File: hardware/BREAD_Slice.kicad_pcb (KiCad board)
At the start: 2 copper layers, 70 x 100 mm, 54 parts, among them J1 1985195, J4 Conn_01x10_Socket, J5 1990106, J6 1990106, Q1 NTGS4111PT1G, SW1 SW_SPDT, SW2 SW_DIP_x04, U1 AP63205, U2 LTV-817S, U3 LTV-817S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

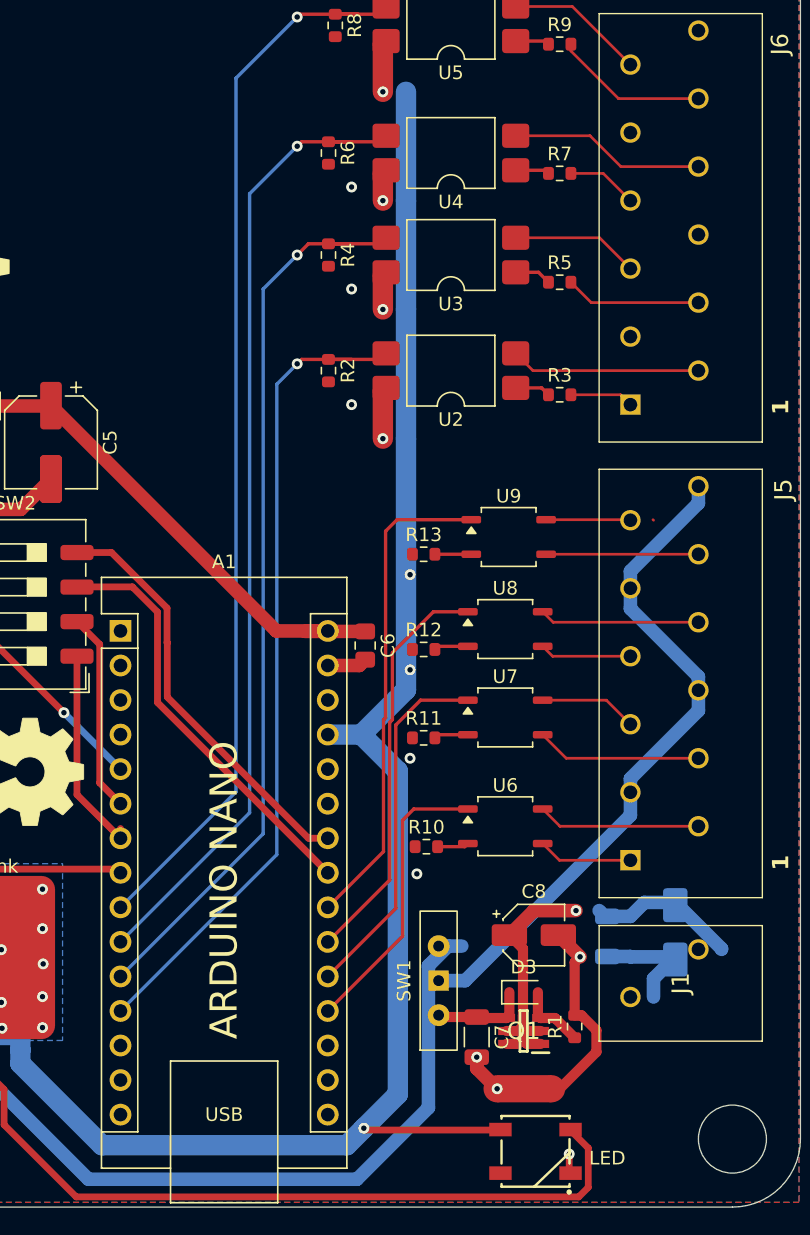
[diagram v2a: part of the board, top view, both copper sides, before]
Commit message: rerouted again with new kml library
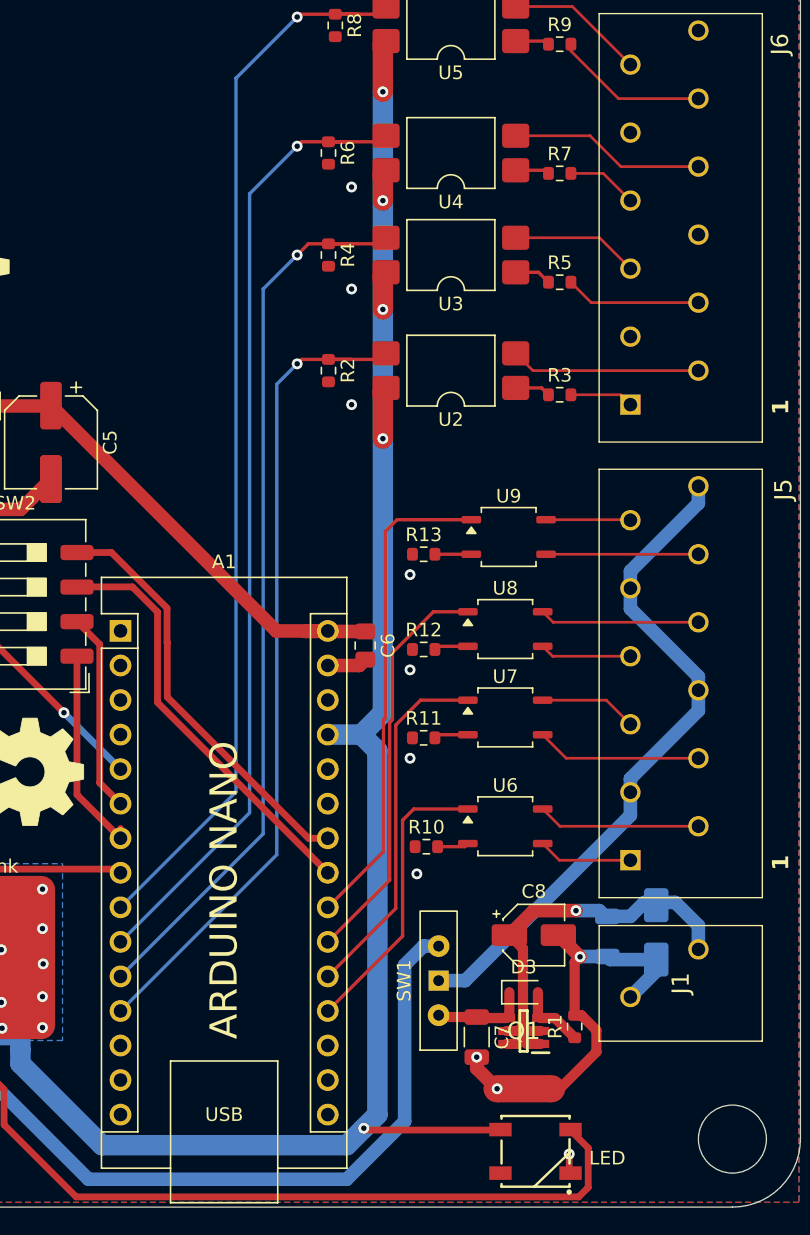
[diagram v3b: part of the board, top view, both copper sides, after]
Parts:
- moved D4 1.40 mm to (182.0, 119.6)
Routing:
- net +5V: track 157.7 -> 155.7 mm
- net +12V: track 118.5 -> 117.4 mm
- net /Input Power Protection/INPUT_VDD: track 32.1 -> 33.1 mm
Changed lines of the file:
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@@
 	(footprint "Diode_SMD:D_SMA"
 		(layer "B.Cu")
-		(at 183.4 119.6 -90)
+		(at 182 119.6 -90)
 		(descr "Diode SMA (DO-214AC)")
 		(tags "Diode SMA (DO-214AC)")
@@
 	)
 	(segment
-		(start 123.95 102.3)
-		(end 126.525 104.875)
-		(width 1.5)
+		(start 140.25 137.75)
+		(end 159.25 137.75)
+		(width 1)
 		(layer "B.Cu")
 		(net 4)
 	)
 	(segment
-		(start 165.25 122.05)
-		(end 166.69 120.61)
-		(width 1)
+		(start 123.95 102.3)
+		(end 126.525 104.875)
+		(width 1.5)
 		(layer "B.Cu")
 		(net 4)
@@
 	)
 	(segment
-		(start 160 137.75)
-		(end 165.25 132.5)
-		(width 1)
-		(layer "B.Cu")
-		(net 4)
-	)
-	(segment
 		(start 126.2 80.89)
 		(end 125.56 80.89)
@@
 	)
 	(segment
-		(start 125.25 123.901649)
-		(end 125.25 127.25)
+		(start 127.34665 121.804999)
+		(end 125.25 123.901649)
+		(width 1)
+		(layer "B.Cu")
+		(net 4)
+	)
+	(segment
+		(start 163.5 133.5)
+		(end 163.5 122)
 		(width 1)
 		(layer "B.Cu")
@@
 	)
 	(segment
+		(start 125.25 123.901649)
+		(end 125.25 127.25)
+		(width 1)
+		(layer "B.Cu")
+		(net 4)
+	)
+	(segment
 		(start 127.6125 119.7875)
 		(end 127.325 119.5)
@@
 	)
 	(segment
-		(start 166.69 120.61)
-		(end 167.7 120.61)
+		(start 127.6125 121.805)
+		(end 127.6125 119.7875)
 		(width 1)
 		(layer "B.Cu")
@@
 	)
 	(segment
-		(start 127.6125 121.805)
-		(end 127.6125 119.7875)
+		(start 131.101 128.601)
+		(end 140.25 137.75)
 		(width 1)
 		(layer "B.Cu")
@@
 	)
 	(segment
-		(start 126.5 128.5)
-		(end 128.305083 128.5)
-		(width 1)
+		(start 126.525 104.875)
+		(end 126.525 118.7)
+		(width 1.5)
 		(layer "B.Cu")
 		(net 4)
 	)
 	(segment
-		(start 131.101 128.601)
-		(end 140.25 137.75)
+		(start 163.5 122)
+		(end 164.89 120.61)
 		(width 1)
 		(layer "B.Cu")
@@
 	)
 	(segment
-		(start 126.525 104.875)
-		(end 126.525 118.7)
-		(width 1.5)
+		(start 125.25 127.25)
+		(end 126.5 128.5)
+		(width 1)
 		(layer "B.Cu")
 		(net 4)
@@
 	)
 	(segment
-		(start 127.34665 121.804999)
-		(end 125.25 123.901649)
-		(width 1)
-		(layer "B.Cu")
-		(net 4)
-	)
-	(segment
 		(start 128.406083 128.601)
 		(end 131.101 128.601)
@@
 	)
 	(segment
-		(start 125.25 127.25)
-		(end 126.5 128.5)
+		(start 164.89 120.61)
+		(end 166 120.61)
+		(width 1)
+		(layer "B.Cu")
+		(net 4)
+	)
+	(segment
+		(start 159.25 137.75)
+		(end 163.5 133.5)
 		(width 1)
 		(layer "B.Cu")
@@
 	)
 	(segment
-		(start 165.25 132.5)
-		(end 165.25 122.05)
-		(width 1)
-		(layer "B.Cu")
-		(net 4)
-	)
-	(segment
-		(start 140.25 137.75)
-		(end 160 137.75)
+		(start 126.5 128.5)
+		(end 128.305083 128.5)
 		(width 1)
 		(layer "B.Cu")
@@
 	)
 	(segment
-		(start 163 107.75)
-		(end 160.31 105.06)
-		(width 1.5)
-		(layer "B.Cu")
-		(net 5)
-	)
-	(segment
 		(start 135.3 116.48)
 		(end 135.3 119.43)
@@
 	)
 	(segment
-		(start 163 131.5)
-		(end 163 107.75)
-		(width 1.5)
-		(layer "B.Cu")
-		(net 5)
-	)
-	(segment
-		(start 163.6 73.8)
-		(end 163.6 65.8)
-		(width 1.5)
-		(layer "B.Cu")
-		(net 5)
-	)
-	(segment
 		(start 135.3 119.43)
 		(end 135.325 119.455)
@@
 	)
 	(segment
-		(start 163.6 101.77)
-		(end 163.6 83.3)
+		(start 161.9 103.47)
+		(end 160.31 105.06)
 		(width 1.5)
 		(layer "B.Cu")
@@
 	)
 	(segment
-		(start 160.5 134)
-		(end 163 131.5)
-		(width 1.5)
-		(layer "B.Cu")
-		(net 5)
-	)
-	(segment
 		(start 159.25 135.25)
 		(end 141.25 135.25)
@@
 	)
 	(segment
-		(start 163.6 65.8)
-		(end 163.6 57.8)
-		(width 1.5)
-		(layer "B.Cu")
-		(net 5)
-	)
-	(segment
-		(start 160.31 105.06)
-		(end 163.6 101.77)
+		(start 160.5 134)
+		(end 161.5 133)
 		(width 1.5)
 		(layer "B.Cu")
@@
 	)
 	(segment
-		(start 163.6 83.3)
-		(end 163.6 73.8)
+		(start 160.5 134)
+		(end 159.25 135.25)
 		(width 1.5)
 		(layer "B.Cu")
@@
 	)
 	(segment
-		(start 160.5 134)
-		(end 159.25 135.25)
+		(start 161.9 57.8)
+		(end 161.9 103.47)
+		(width 1.5)
+		(layer "B.Cu")
+		(net 5)
+	)
+	(segment
+		(start 161.5 133)
+		(end 161.5 106.25)
+		(width 1.5)
+		(layer "B.Cu")
+		(net 5)
+	)
+	(segment
+		(start 161.5 106.25)
+		(end 160.31 105.06)
 		(width 1.5)
 		(layer "B.Cu")
@@
 	)
 	(segment
+		(start 177.8 118)
+		(end 176.1 118)
+		(width 1)
+		(layer "B.Cu")
+		(net 43)
+	)
+	(segment
 		(start 183.4 117.4)
 		(end 181.125 117.4)
@@
 	)
 	(segment
-		(start 186.8 120.85)
-		(end 186.8 120.8)
+		(start 183.4 117.4)
+		(end 185.1 119.1)
 		(width 1)
 		(layer "B.Cu")
@@
 	)
 	(segment
-		(start 186.8 120.8)
-		(end 183.4 117.4)
+		(start 185.1 119.1)
+		(end 185.1 120.85)
 		(width 1)
 		(layer "B.Cu")
@@
 	)
 	(segment
-		(start 181.8 124.35)
-		(end 181.8 123)
+		(start 176.425 121.375)
+		(end 176.4 121.4)
 		(width 1)
 		(layer "B.Cu")
@@
 	)
 	(segment
-		(start 183.4 121.4)
-		(end 180.125 121.4)
+		(start 182 121.6)
+		(end 182 122.45)
 		(width 1)
 		(layer "B.Cu")
@@
 	)
 	(segment
-		(start 178.125 121.375)
-		(end 178.1 121.4)
+		(start 182 121.6)
+		(end 178.625 121.6)
 		(width 1)
 		(layer "B.Cu")
@@
 	)
 	(segment
-		(start 181.8 123)
-		(end 183.4 121.4)
+		(start 178.625 121.6)
+		(end 178.4 121.375)
 		(width 1)
 		(layer "B.Cu")
@@
 	)
 	(segment
-		(start 180.1 121.375)
+		(start 178.1 121.4)
 		(end 178.125 121.375)
 		(width 1)
@@
 	)
 	(segment
-		(start 180.125 121.4)
-		(end 180.1 121.375)
+		(start 178.4 121.375)
+		(end 176.425 121.375)
+		(width 1)
+		(layer "B.Cu")
+		(net 44)
+	)
+	(segment
+		(start 182 122.45)
+		(end 180.1 124.35)
 		(width 1)
 		(layer "B.Cu")
@@
 		(width 0.2)
 		(layer "F.Cu")
-		(net 50)
-	)
-	(segment
-		(start 181.76 89.26)
-		(end 181.8 89.3)
-		(width 0.2)
-		(layer "F.Cu")

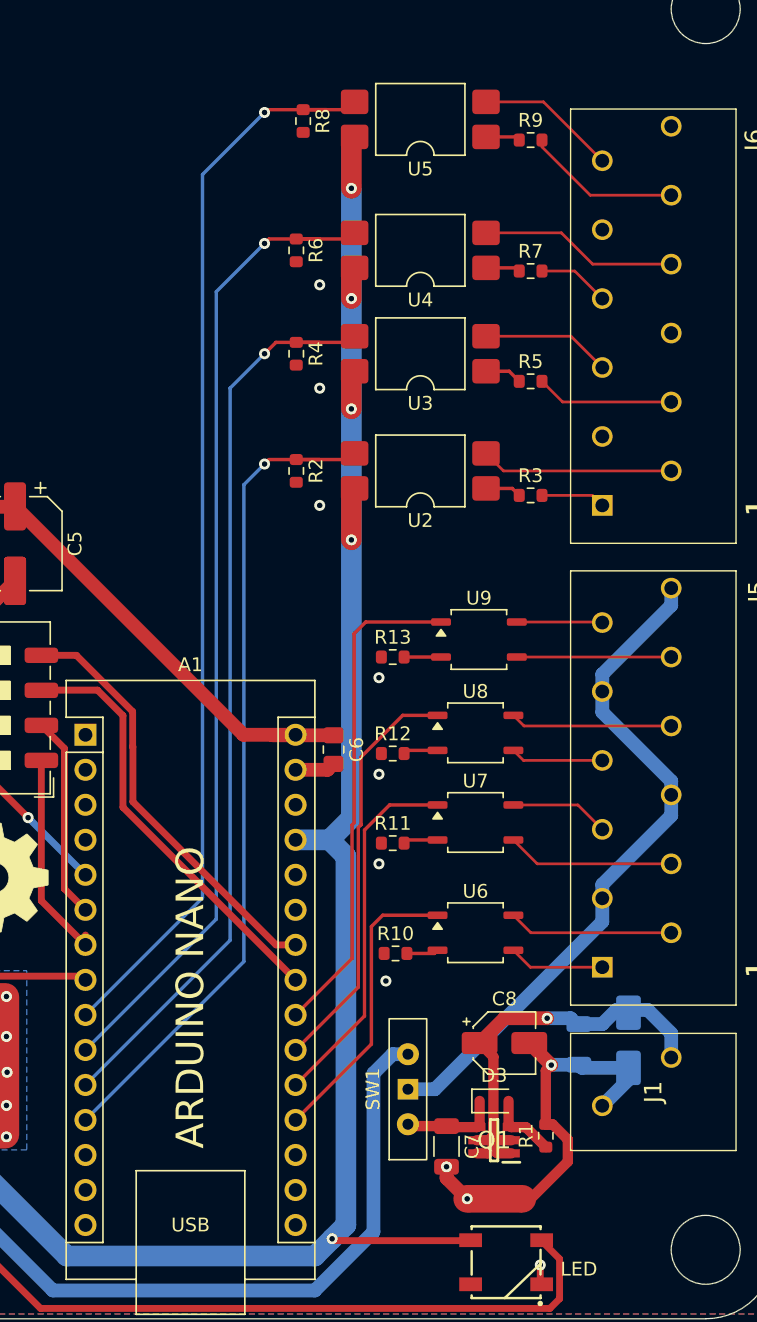
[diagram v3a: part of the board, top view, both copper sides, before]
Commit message: update all to KMLib, untrack backups in gitignore, and revise routing on board to simplify
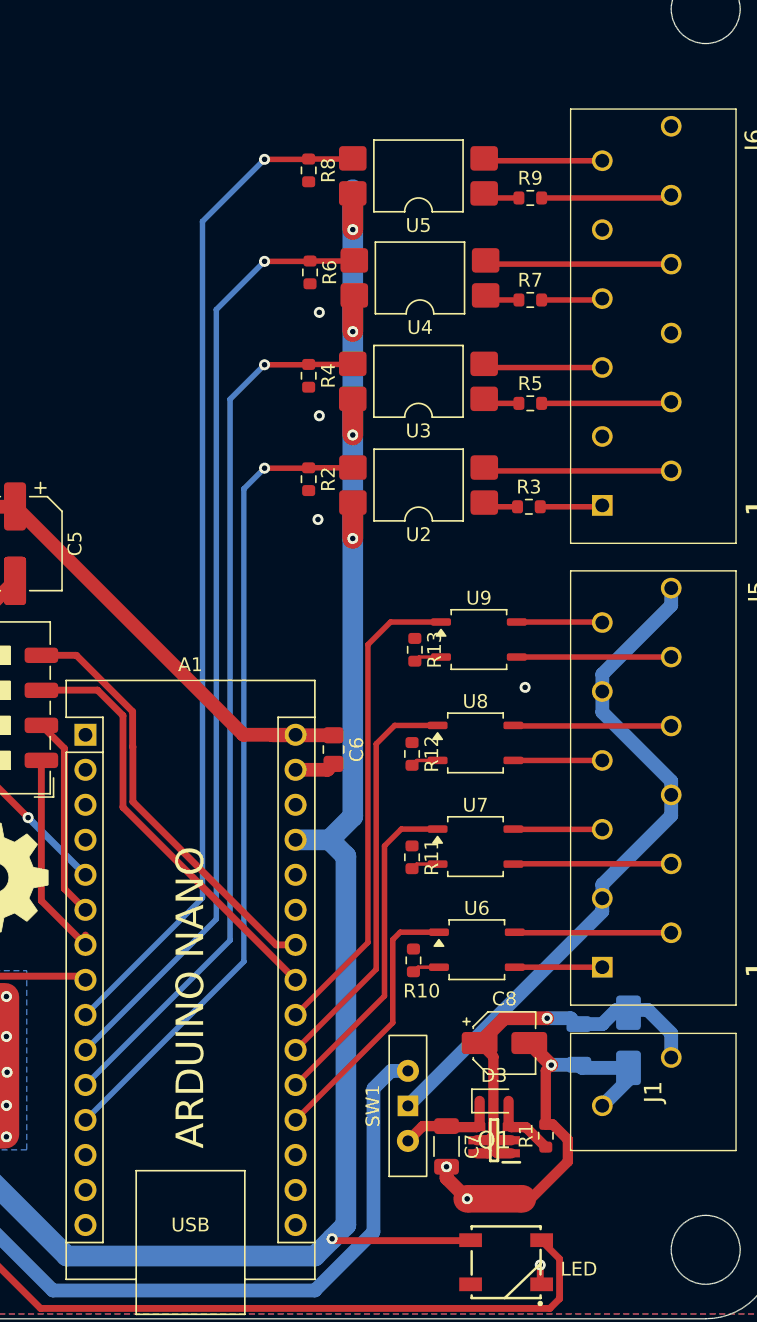
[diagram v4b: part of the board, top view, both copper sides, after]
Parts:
- moved R9 4.20 mm to (174.9, 58.5)
- moved U5 4.10 mm to (166.8, 56.9)
- moved R8 3.60 mm to (158.8, 56.5)
- moved R7 2.10 mm to (174.9, 65.9)
- moved U3 2.00 mm to (166.8, 71.8)
- moved U4 2.00 mm to (166.9, 64.3)
- moved R6 1.89 mm to (158.9, 63.9)
- moved R4 1.84 mm to (158.8, 71.4)
- moved U7 1.75 mm to (170.9, 105.5)
- moved R11 1.74 mm to (166.3, 106.3), turned to -90 degrees
- moved R13 1.68 mm to (166.5, 91.3), turned to -90 degrees
- moved R5 1.60 mm to (174.9, 73.4)
- moved R12 1.40 mm to (166.3, 98.8), turned to -90 degrees
- moved R10 1.39 mm to (166.4, 113.8), turned to -90 degrees
- moved U6 1.23 mm to (171.0, 113.0)
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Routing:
- net /IN4: track 79.4 -> 73.9 mm
- net /IN3: track 72.4 -> 69.1 mm
- net /IN2: track 67.2 -> 64.0 mm
- net +5V: track 155.7 -> 153.3 mm
- net /IN1: track 61.5 -> 59.1 mm
- net /OUT2: track 26.6 -> 24.4 mm
- net /OUT1: track 21.4 -> 19.6 mm
- net /IN4+: track 11.3 -> 9.48 mm
- net /IN4-: track 10.2 -> 8.53 mm
- net +12V: track 117.4 -> 116.2 mm
- net /OUT4: track 36.1 -> 35.0 mm
- net /IN2-: track 9.38 -> 8.57 mm
- net /IN3-: track 14.4 -> 13.6 mm
- net /IN3+: track 5.20 -> 4.44 mm
- net /OUT2+: track 12.2 -> 11.4 mm
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
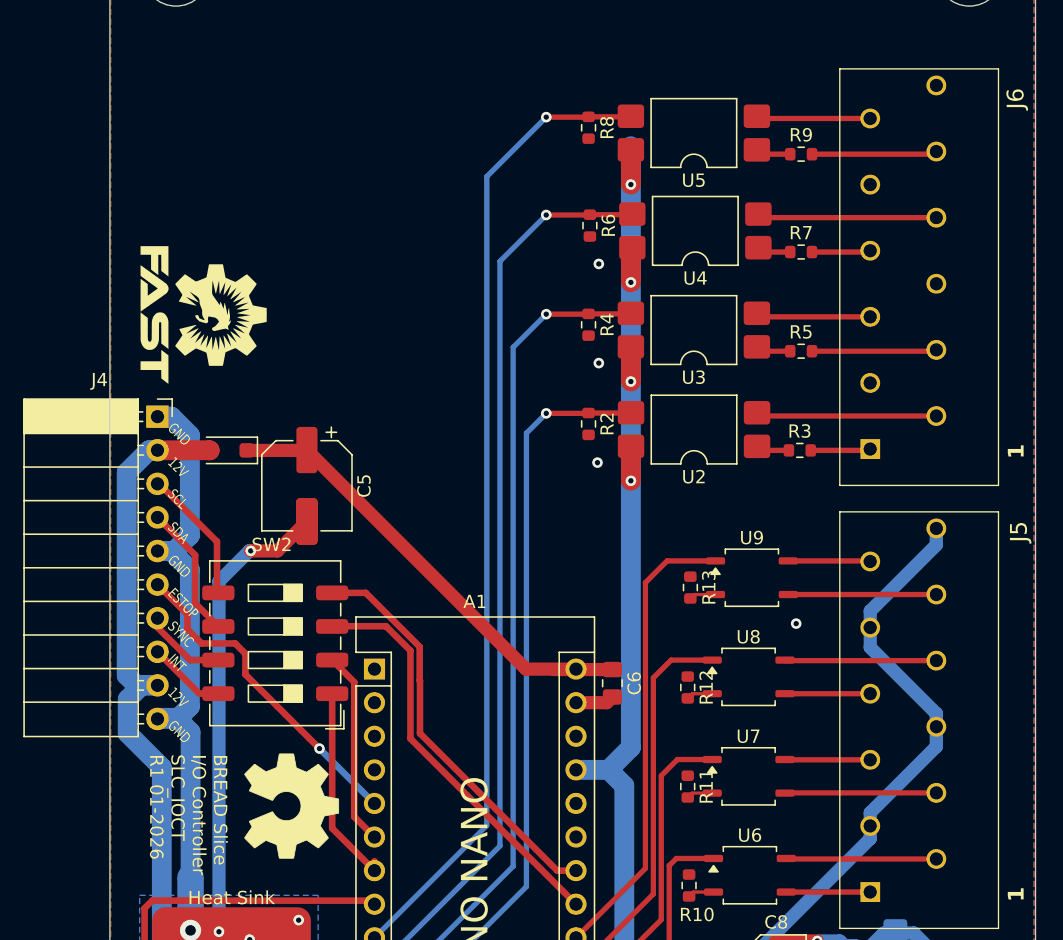
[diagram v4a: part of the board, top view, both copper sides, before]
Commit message: added dip switches to IOCT
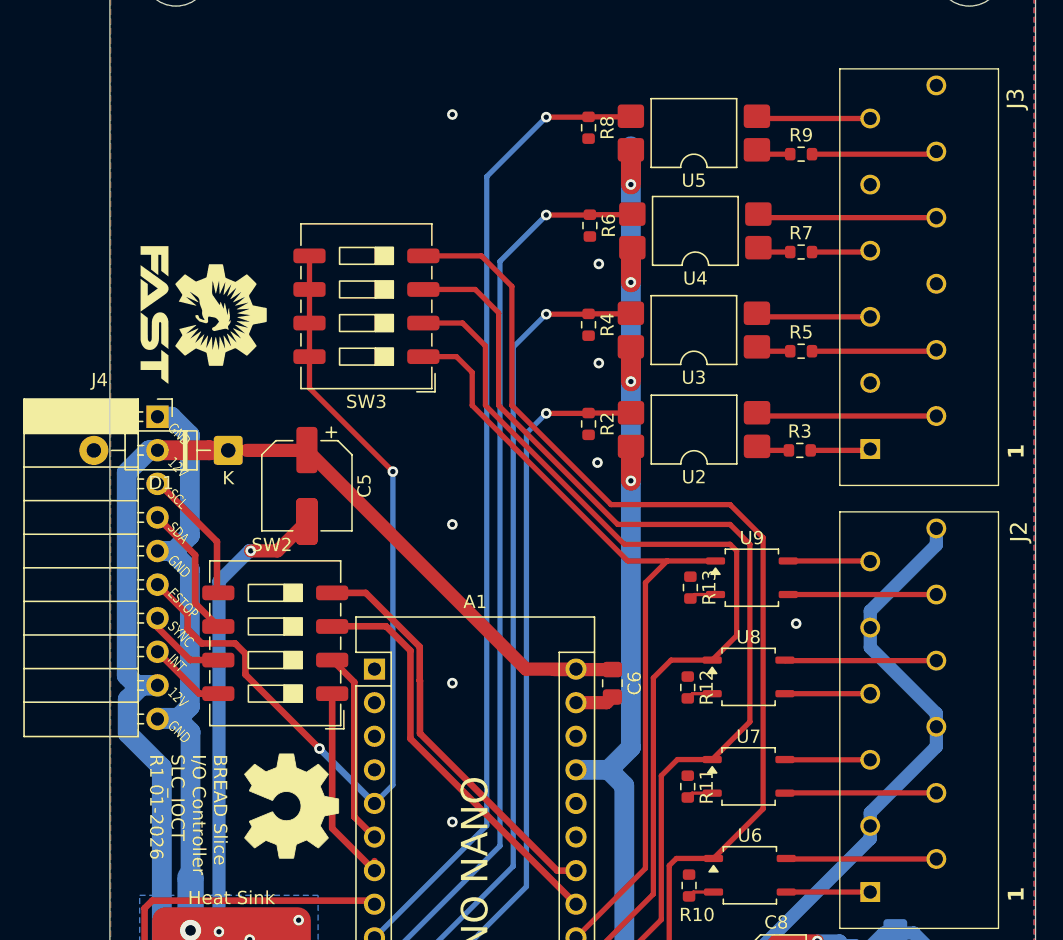
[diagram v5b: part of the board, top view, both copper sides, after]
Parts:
- added SW3: SW_DIP_x04, Button_Switch_SMD:SW_DIP_SPSTx04_Slide_9.78x12.34mm_W8.61mm_P2.54mm, F.Cu at (142.0, 70.0)
- A1: footprint KMLib_Boards_Modules:Arduino_Nano_Headers -> KMLib_Boards_Modules:Arduino_Nano
- D1: footprint Diode_SMD:D_SOD-123F -> Diode_THT:D_DO-41_SOD81_P10.16mm_Horizontal
- renumbered J5 to J2, J6 to J3
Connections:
- net /slice_template/ESTOP renamed /ESTOP
- net /slice_template/I2C_CLK/A5 renamed /I2C_CLK
- net /slice_template/I2C_DAT/A4 renamed /I2C_DAT
- SW1 pad 1: /VFIELD -> +12V
- SW1 pad 2: /+24V -> /VFIELD
- SW1 pad 3: +12V -> /+24V
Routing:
- net /OUT1: track 19.6 -> 85.2 mm
- net /OUT2: track 24.4 -> 78.6 mm
- net /ESTOP: track 25.9 -> 70.5 mm, vias 1 -> 2
- net /OUT3: track 29.6 -> 72.1 mm
- net /OUT4: track 35.0 -> 61.3 mm
- net GND: vias 25 -> 29
